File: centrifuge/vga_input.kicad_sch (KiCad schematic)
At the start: 0 parts

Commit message: Completed majority of schematic, need to add decoupling but otherwise mostly ready
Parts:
- added C70, C? (x7): 0.1u, Capacitor_SMD:C_0805_2012Metric_Pad1.18x1.45mm_HandSolder, symbol Device:C_Small
- added C? (x3): 1n, Capacitor_SMD:C_0805_2012Metric_Pad1.18x1.45mm_HandSolder, symbol Device:C_Small
- added C? (x11): 1u, Capacitor_SMD:C_0805_2012Metric_Pad1.18x1.45mm_HandSolder, symbol Device:C_Small
- added C? (x7): 10n, Capacitor_SMD:C_0805_2012Metric_Pad1.18x1.45mm_HandSolder, symbol Device:C_Small
- added C?: 4.7n, Capacitor_SMD:C_0805_2012Metric_Pad1.18x1.45mm_HandSolder, symbol Device:C_Small
- added JP?: Jumper_3_Open, Jumper:SolderJumper-3_P1.3mm_Open_Pad1.0x1.5mm_NumberLabels, symbol Jumper:Jumper_3_Open
- added R45: 10k, Resistor_SMD:R_0805_2012Metric_Pad1.20x1.40mm_HandSolder, symbol Device:R_Small
- added R? (x4): 2.2k, Resistor_SMD:R_0805_2012Metric_Pad1.20x1.40mm_HandSolder, symbol Device:R_Small
- added R?: 1.5k, Resistor_SMD:R_0805_2012Metric_Pad1.20x1.40mm_HandSolder, symbol Device:R_Small
- added U?: TVP7002, Package_QFP:TQFP-100-1EP_14x14mm_P0.5mm_EP5x5mm_ThermalVias, symbol centrifuge_symbols:TVP7002
- added X?: ECS-2333-270-BN, Oscillator:Oscillator_SMD_EuroQuartz_XO32-4Pin_3.2x2.5mm_HandSoldering, symbol centrifuge_symbols:ECS-2333-xxx-xx
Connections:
- new net: C?.1, U?.97 (SOGIN_3)
- new net: JP?.3 (B), R?.1
- new net: C?.1, U?.11 (RIN_1)
- new net: R45.2, X?.1 (Tri-State)
- new net: U?.80 (EXT_CLK), X?.3 (OUT)
- new net: JP?.1 (A), R?.2
- new net: JP?.2 (C), U?.73 (I2CA)
- new net: C?.1, U?.16 (BIN_3)
- new net: C?.1, U?.98 (GIN_3)
- new net: C?.2, R?.1
- new net: R?.2, U?.87 (FILT1)
- new net: C?.1, U?.1 (SOGIN_1)
- new net: C?.1, U?.10 (RIN_2)
- new net: C?.1, U?.100 (GIN_2)
- new net: C?.1, U?.17 (BIN_2)
- new net: C?.1, U?.18 (BIN_1)
- new net: C?.1, U?.2 (GIN_1)
- new net: C?.2, U?.88 (FILT2)
- new net: C?.1, C?.1, U?.89 (PLL_F)
- new net: C?.1, U?.9 (RIN_3)
- new net: C?.1, U?.96 (GIN_4)
- new net: C?.1, U?.99 (SOGIN_2)
- new net +1V8: C?.1, C?.1, C?.1, C?.1, C?.1, C?.1, U?.19 (AVDD), U?.39 (DVDD), U?.4 (AVDD), U?.6 (AVDD), U?.69 (DVDD), U?.7 (AVDD), U?.84 (PLL_AVDD), U?.85 (PLL_AVDD)
- new net +3.3VA: C70.1, C?.1, C?.1, C?.1, C?.1, C?.1, C?.1, C?.1, C?.1, R45.1, R?.1, R?.1, R?.1, U?.13 (A33VDD), U?.14 (A33VDD), U?.26 (IOVDD), U?.41 (IOVDD), U?.53 (IOVDD), U?.66 (IOVDD), U?.93 (A33VDD), U?.94 (A33VDD), X?.4 (VDD)
- new net B: C?.2
- new net B5: U?.33 (B_5)
- new net B6: U?.32 (B_6)
- new net B7: U?.31 (B_7)
- new net B8: U?.30 (B_8)
- new net B9: U?.29 (B_9)
- new net DCLK_OUT: U?.28 (DATACLK)
- new net FIDOUT: U?.22 (FIDOUT)
- new net G: C?.2
- new net G4: U?.48 (G_4)
- new net G5: U?.47 (G_5)
- new net G6: U?.46 (G_6)
- new net G7: U?.45 (G_7)
- new net G8: U?.44 (G_8)
- new net G9: U?.43 (G_9)
- new net GND: C70.2, C?.2, C?.2, C?.2, C?.2, C?.2, C?.2, C?.2, C?.2, C?.2, C?.2, C?.2, C?.2, C?.2, C?.2, C?.2, C?.2, C?.2, C?.2, C?.2, C?.2, C?.2, C?.2, C?.2, C?.2, R?.2, U?.12 (A33GND), U?.15 (A33GND), U?.20 (AGND), U?.21 (NSUB), U?.27 (IOGND), U?.3 (AGND), U?.40 (GND), U?.42 (IOGND), U?.5 (AGND), U?.54 (IOGND), U?.60 (IOGND), U?.67 (IOGND), U?.68 (GND), U?.70 (PWDN), U?.72 (TMS), U?.76 (CLAMP), U?.77 (COAST), U?.79 (VSYNC_B), U?.8 (AGND), U?.82 (HSYNC_B), U?.83 (PLL_AGND), U?.86 (PLL_AGND), U?.90 (PLL_AGND), U?.91 (NSUB), U?.92 (A33GND), U?.95 (A33GND), X?.2 (GND)
- new net HSIN: U?.81 (HSYNC_A)
- new net HSOUT: U?.24 (HSOUT)
- new net R: C?.2
- new net R5: U?.59 (R_5)
- new net R6: U?.58 (R_6)
- new net R7: U?.57 (R_7)
- new net R8: U?.56 (R_8)
- new net R9: U?.55 (R_9)
- new net RESET: U?.71 (RESETB)
- new net SCL: R?.2, U?.74 (SCL)
- new net SDA: R?.2, U?.75 (SDA)
- new net VSOUT: U?.23 (VSOUT)
- no-connect marks 0 -> 15
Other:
- note added: "This one is supposed to be a separate rail."
- title: (none) -> VGA Centrifuge

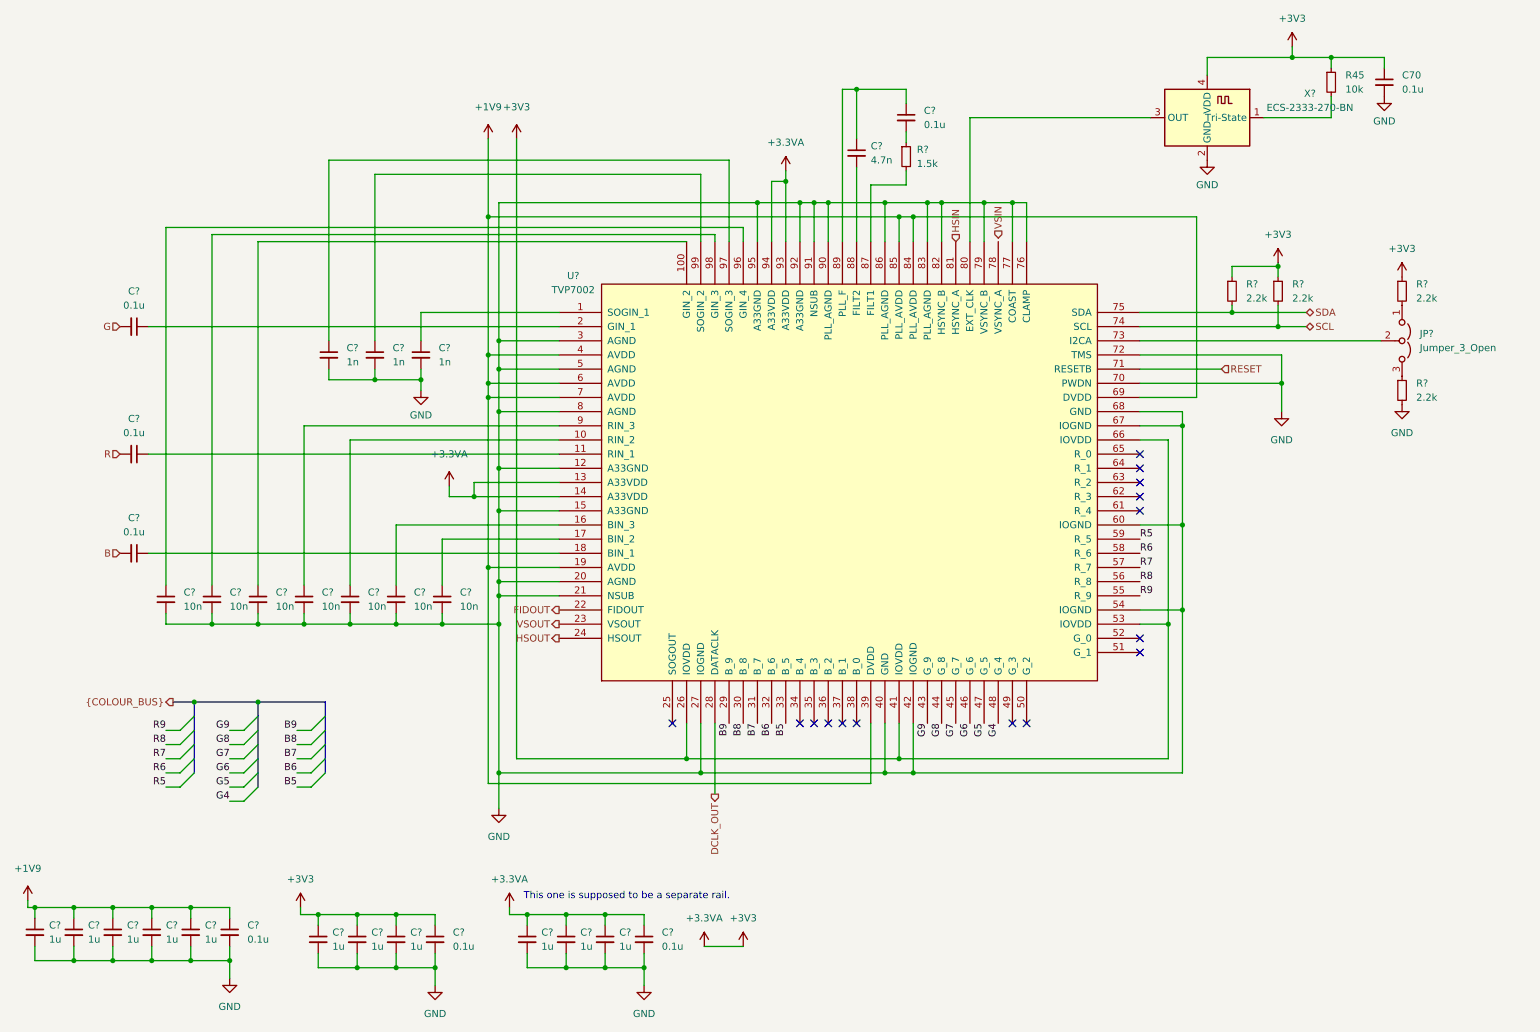
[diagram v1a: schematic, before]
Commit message: FPGA PCB design completed
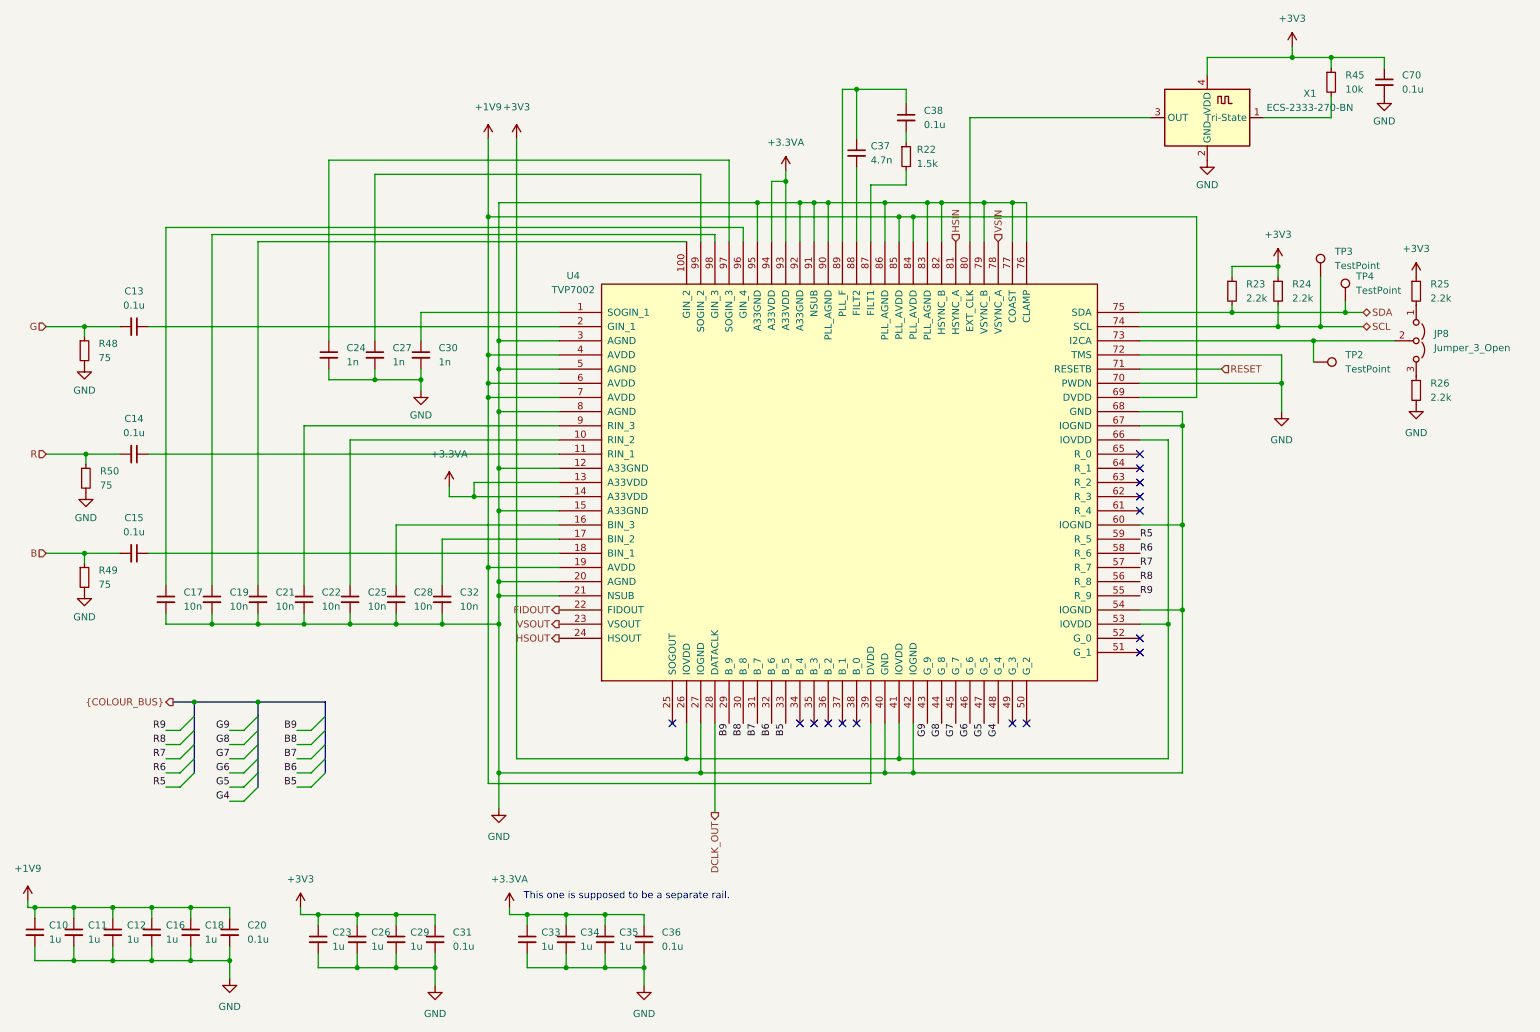
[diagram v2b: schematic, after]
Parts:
- added R48, R49, R50: 75, Resistor_SMD:R_0805_2012Metric_Pad1.20x1.40mm_HandSolder, symbol Device:R_Small
- added TP2, TP3, TP4: TestPoint, TestPoint:TestPoint_Keystone_5015_Micro-Minature, symbol Connector:TestPoint
- U4: renamed from U?; footprint Package_QFP:TQFP-100-1EP_14x14mm_P0.5mm_EP5x5mm_ThermalVias -> centrifuge footprints:TQFP-100-1EP_14x14mm_P0.5mm_EP5x5mm_ThermalVias_elprint
- gave numbers to parts that had none: 36
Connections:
- net +3.3VA: no longer C23.1, C26.1, C29.1, C31.1, C70.1, R23.1, R24.1, R25.1, R45.1, U4.26 (IOVDD), U4.41 (IOVDD), U4.53 (IOVDD), U4.66 (IOVDD), X1.4 (VDD)
- net B: now also R49.1
- net G: now also R48.1
- net R: now also R50.1
- net SCL: now also TP3.1
- net SDA: now also TP4.1
- net VSIN: now also U4.78 (VSYNC_A)
- net at JP8.2 (C), U4.73 (I2CA): now also TP2.1
- net +1V8 renamed +1V9
- net GND renamed EP_GND
- net EP_GND: now also U4.101 (EP_GND), R48.2, R49.2, R50.2
- new net +3V3: C23.1, C26.1, C29.1, C31.1, C70.1, R23.1, R24.1, R25.1, R45.1, U4.26 (IOVDD), U4.41 (IOVDD), U4.53 (IOVDD), U4.66 (IOVDD), X1.4 (VDD)
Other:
- moved on the sheet: JP8, R25, R26
